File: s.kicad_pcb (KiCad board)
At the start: 2 copper layers, 200 x 77.4 mm, 98 parts, among them J2 UART connector, J4 Conn_01x02_Pin, J5 USB4105-GF-A, SW1 Z, SW10 D, SW11 S, SW12 K, SW13 W, SW14 R, SW15 STAR, SW16 R, SW17 B, SW18 G, SW19 S, SW2 T, SW20 Z, SW21 A, SW22 O, SW23 NUM, SW24 E, SW25 U, SW26 210-4MS, SW27 09.03290.01, SW28 EVP-AA202K, SW3 P, SW4 H, SW5 STAR, SW6 F, SW7 P, SW8 L, SW9 T, U1 ESP32-S3-WROOM-1, U2 MCP1825S, U3 MCP1825S, U4 AP9101CK, U5 MCP73831-2-OT, U6 DMG6968U-7, U7 DMG6968U-7

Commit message: WIP: drafting PCB edges
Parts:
- J2: moved to B.Cu
- moved H4 201.1 mm to (56.6, 131.6)
- moved H3 141.2 mm to (204.7, 131.6)
- moved H1 77.0 mm to (238.9, 63.1)
- moved J2 33.2 mm to (224.4, 95.8)
- moved C4 18.2 mm to (197.4, 117.4)
- moved C2 18.0 mm to (197.4, 115.2)
- moved R3 16.9 mm to (197.4, 119.9)
- moved SW27 16.8 mm to (73.2, 120.7)
- moved J4 15.5 mm to (69.6, 105.6)
- moved J5 10.5 mm to (56.0, 120.3)
- moved C6 8.72 mm to (219.4, 123.8)
- moved U2 8.47 mm to (204.0, 122.2)
- moved C5 8.41 mm to (216.7, 123.8)
- moved R1 8.41 mm to (214.0, 123.8)
- moved C1 8.41 mm to (210.9, 124.8)
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- renumbered H2 to H1, H4 to H2, H5 to H3, H6 to H4
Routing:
- net /battery_mgmt/vbatt_mon: track 193.2 -> 0.00 mm, vias 2 -> 0
- net /VBUS: track 173.1 -> 0.00 mm, vias 2 -> 0
- net Net-(U1-IO16): track 160.7 -> 0.00 mm, vias 2 -> 0
- net /battery_mgmt/3v3_from_batt: track 146.4 -> 0.00 mm, vias 2 -> 0
- net +3.3V: track 129.2 -> 23.1 mm, vias 2 -> 0
- net Net-(U1-IO0): track 72.2 -> 2.68 mm, vias 1 -> 0
- net /sw_2: track 68.7 -> 0.00 mm, vias 1 -> 0
- net /battery_mgmt/HV_CHR: track 68.3 -> 0.00 mm
- net /sw_3: track 66.6 -> 0.00 mm, vias 1 -> 0
- net /sw_4: track 64.1 -> 0.00 mm, vias 1 -> 0
- net /matrix_c5: track 148.2 -> 91.5 mm, vias 1 -> 0
- net /matrix_c4: track 167.1 -> 110.9 mm, vias 1 -> 0
- net /USB_D+: track 183.8 -> 127.7 mm
- net /led_2: track 87.2 -> 31.5 mm, vias 1 -> 0
- net /USB_D-: track 182.6 -> 127.7 mm
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- removed copper zone on B.Cu, net GND
- removed copper zone on F.Cu, net GND
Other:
- board size 200 x 77.4 mm -> 218.3 x 102.6 mm

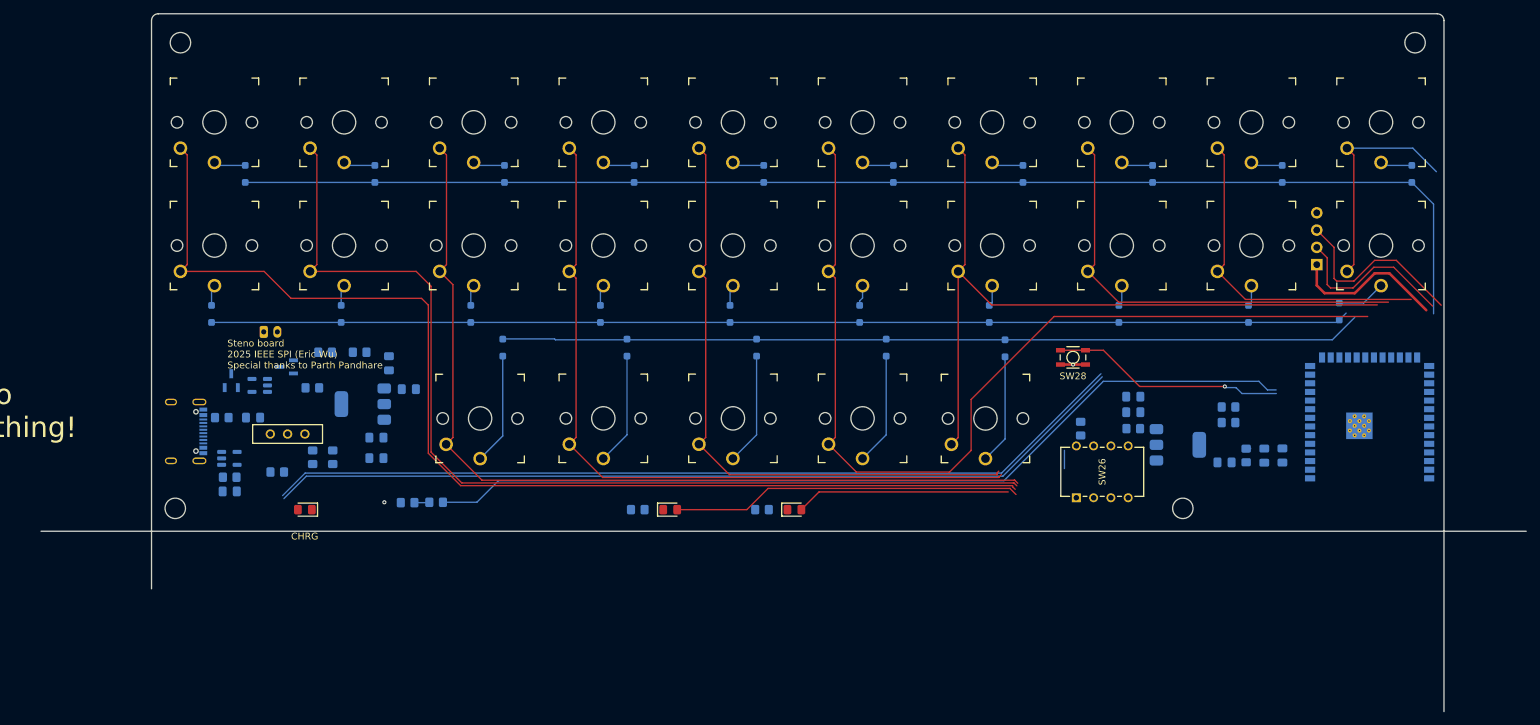
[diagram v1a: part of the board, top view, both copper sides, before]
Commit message: WIP :finalize edge cuts
The new board dimensions are 189.95mm x 76.05mm
with corners of radius 1.00 mm
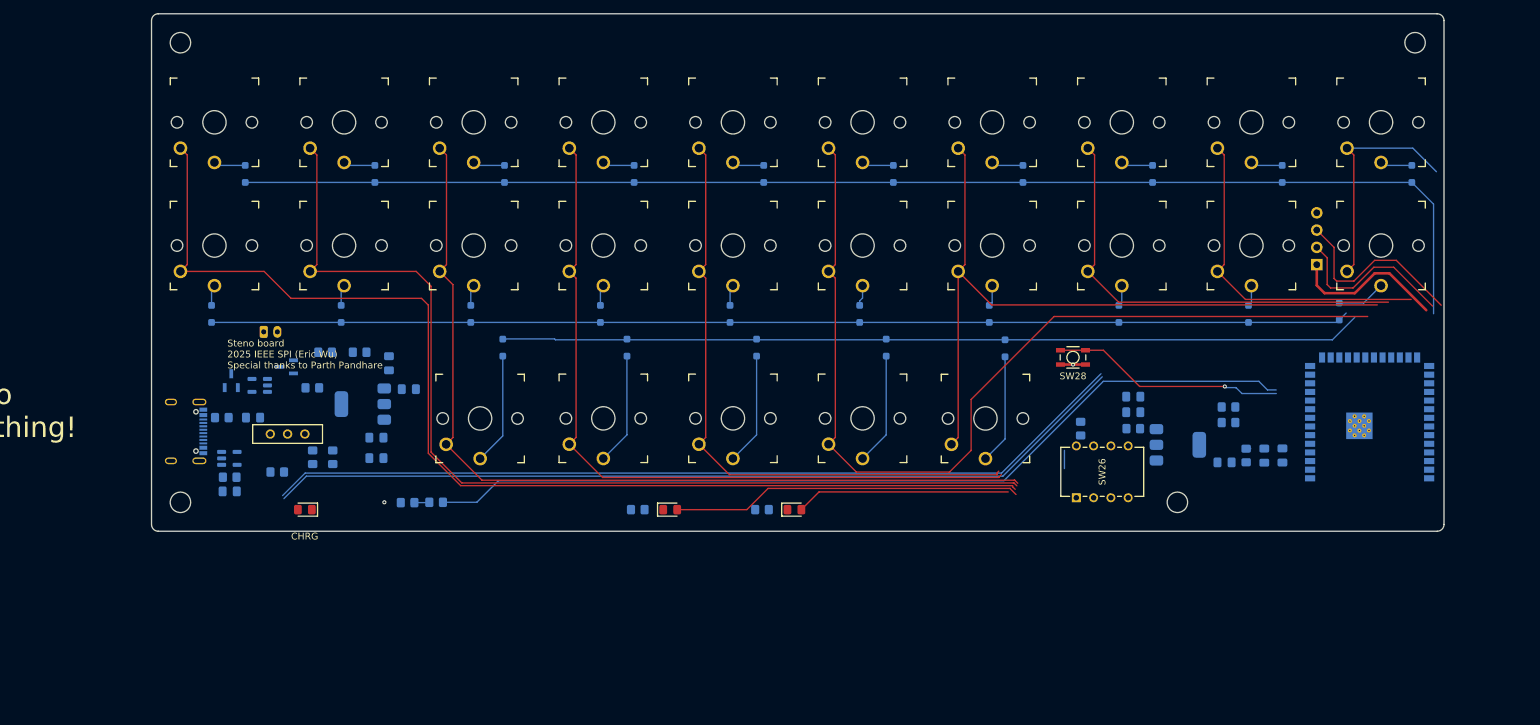
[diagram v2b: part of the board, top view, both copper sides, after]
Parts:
- moved H3 1.19 mm to (203.9, 130.7)
- moved H4 1.17 mm to (57.4, 130.7)
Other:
- board size 218.3 x 102.6 mm -> 190 x 76 mm
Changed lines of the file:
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@@
 	(footprint "MountingHole:MountingHole_3mm"
 		(layer "F.Cu")
-		(at 56.642 131.572)
+		(at 57.404 130.688)
 		(descr "Mounting Hole 3mm, no annular, generated by kicad-footprint-generator mountinghole.py")
 		(tags "mountinghole")
@@
 	(footprint "MountingHole:MountingHole_3mm"
 		(layer "F.Cu")
-		(at 204.724 131.572)
+		(at 203.924 130.688)
 		(descr "Mounting Hole 3mm, no annular, generated by kicad-footprint-generator mountinghole.py")
 		(tags "mountinghole")
@@
 	)
 	(gr_line
-		(start 53.154 143.398875)
+		(start 53.154 133.9375)
 		(end 53.154 59.88775)
 		(stroke
@@
 		(layer "Edge.Cuts")
 	)
+	(gr_arc
+		(start 54.154 134.9375)
+		(mid 53.446893 134.644607)
+		(end 53.154 133.9375)
+		(stroke
+			(width 0.05)
+			(type solid)
+		)
+		(layer "Edge.Cuts")
+	)
 	(gr_line
-		(start 243.104 161.44875)
+		(start 243.104 133.9375)
 		(end 243.104 59.88775)
 		(stroke
@@
 	)
 	(gr_line
-		(start 36.909375 134.9375)
-		(end 255.190625 134.9375)
+		(start 54.154 134.9375)
+		(end 242.104 134.9375)
 		(stroke
 			(width 0.05)
-			(type default)
+			(type solid)
+		)
+		(layer "Edge.Cuts")
+	)
+	(gr_arc
+		(start 243.104 133.9375)
+		(mid 242.811107 134.644607)
+		(end 242.104 134.9375)
+		(stroke
+			(width 0.05)
+			(type solid)
 		)
 		(layer "Edge.Cuts")

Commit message: WIP: routing traces
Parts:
- moved R2 23.6 mm to (212.7, 124.8)
- moved R16 17.4 mm to (96.4, 129.2), turned to 0 degrees
- moved R17 16.2 mm to (92.2, 129.2), turned to 180 degrees
- moved SW27 11.7 mm to (70.7, 109.2)
- moved D25 9.82 mm to (170.8, 114.0)
- moved D20 9.15 mm to (219.5, 98.7)
- moved C1 9.01 mm to (215.3, 117.0), turned to 90 degrees
- moved U7 8.76 mm to (64.6, 113.4), turned to -90 degrees
- moved SW28 8.65 mm to (196.8, 111.9)
- moved D10 7.11 mm to (231.3, 82.4)
- moved D21 6.10 mm to (104.9, 114.0)
- moved D22 6.10 mm to (123.2, 114.0)
- moved D23 6.10 mm to (142.2, 114.0)
- moved D24 6.10 mm to (161.3, 114.0)
- moved R7 5.23 mm to (67.8, 121.2)
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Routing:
- net /battery_mgmt/vbatt_mon: track 0.00 -> 284.5 mm, vias 0 -> 2
- net /VBUS: track 0.00 -> 163.0 mm, vias 0 -> 5
- net Net-(U1-IO16): track 0.00 -> 149.1 mm
- net /battery_mgmt/3v3_from_batt: track 0.00 -> 143.4 mm, vias 0 -> 2
- net GND: track 3.68 -> 140.8 mm, vias 2 -> 5
- net Net-(U1-IO0): track 2.68 -> 72.9 mm, vias 0 -> 2
- net /USB_D+: track 127.7 -> 189.5 mm
- net /USB_D-: track 127.7 -> 188.1 mm, vias 0 -> 2
- net /sw_2: track 0.00 -> 59.6 mm, vias 0 -> 1
- net /sw_3: track 0.00 -> 55.0 mm, vias 0 -> 1
- net /led_2: track 31.5 -> 82.1 mm, vias 0 -> 1
- net /sw_4: track 0.00 -> 50.4 mm, vias 0 -> 1
- net /CC2: track 0.00 -> 50.4 mm
- net /led_1: track 51.5 -> 101.2 mm, vias 0 -> 1
- net /matrix_c4: track 110.9 -> 158.2 mm, vias 0 -> 1
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
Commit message: WIP: more routing done
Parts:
- moved D30 5.62 mm to (71.9, 130.7), turned to 0 degrees
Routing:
- net /matrix_r2: track 161.3 -> 182.0 mm
- net GND: track 140.8 -> 130.2 mm
- net Net-(D30-K): track 11.6 -> 5.34 mm
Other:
- board text added: "Steno board UCLA IEEE SPI (Eric Wu, 2025) Special thanks to Parth Pandhare"
- board text removed: "Steno board 2025 IEEE SPI (Eric Wu) Special thanks to Parth Pandhare"

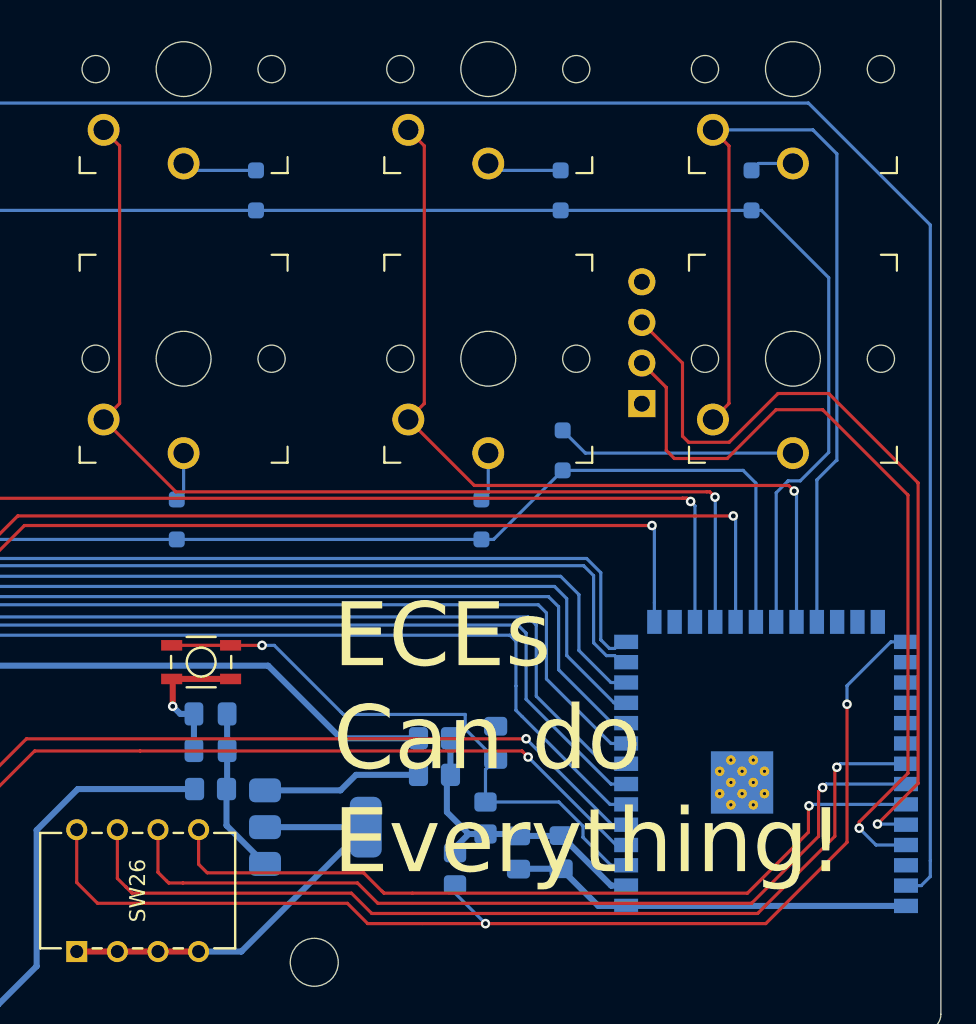
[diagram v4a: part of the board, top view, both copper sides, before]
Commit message: WIP: route everything except ground planes
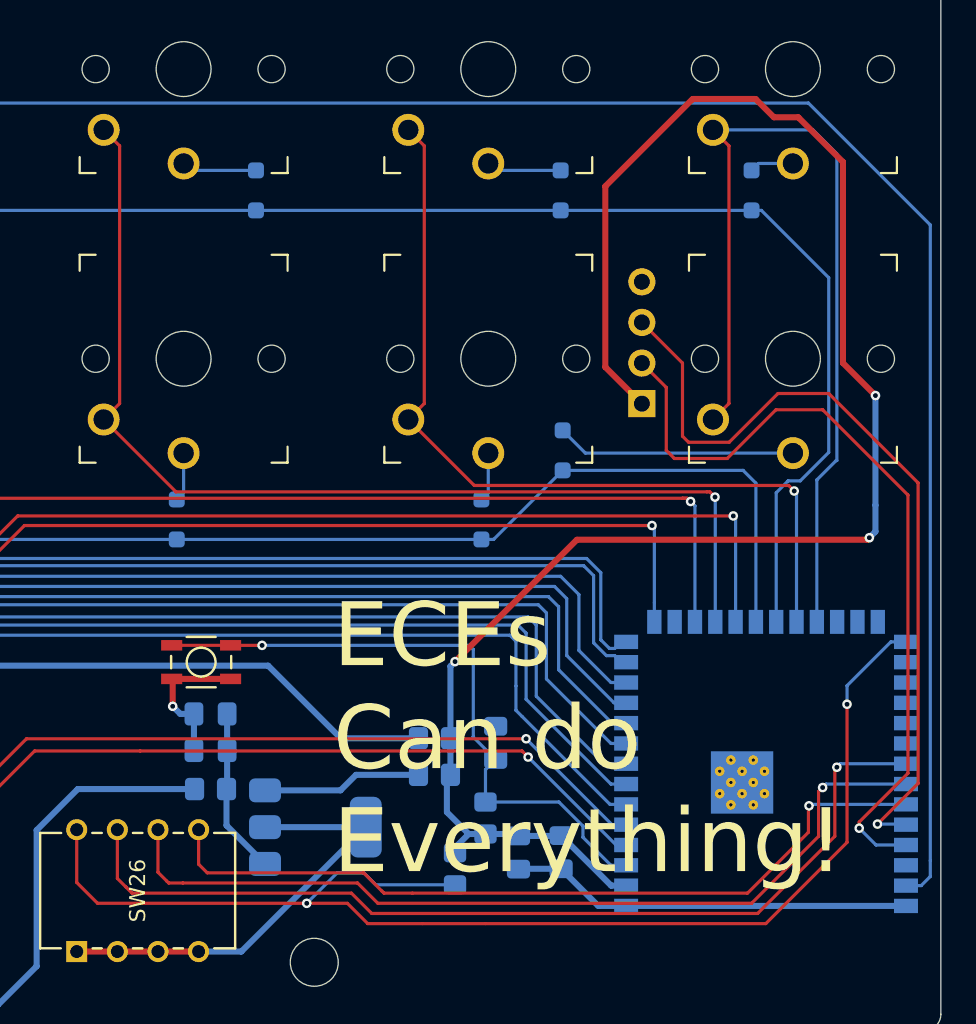
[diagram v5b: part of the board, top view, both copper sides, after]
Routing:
- net +3.3V: track 19.4 -> 111.2 mm, vias 0 -> 3
- net Net-(U1-IO0): track 72.9 -> 80.1 mm
- net Net-(U1-EN): track 37.5 -> 40.2 mm
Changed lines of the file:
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@@
+	)
+	(segment
+		(start 239.014 95.25)
+		(end 236.982 93.218)
+		(width 0.381)
+		(layer "F.Cu")
+		(net 7)
+	)
+	(segment
+		(start 222.123 93.472)
+		(end 224.409 95.758)
+		(width 0.381)
+		(layer "F.Cu")
+		(net 7)
+	)
+	(segment
+		(start 212.725 111.887)
+		(end 218.694 105.918)
+		(width 0.381)
+		(layer "F.Cu")
+		(net 7)
+	)
+	(segment
+		(start 232.664 77.851)
+		(end 231.521 76.708)
+		(width 0.381)
+		(layer "F.Cu")
+		(net 7)
+	)
+	(segment
+		(start 234.188 77.851)
+		(end 232.664 77.851)
+		(width 0.381)
+		(layer "F.Cu")
+		(net 7)
+	)
+	(segment
+		(start 220.345 104.267)
+		(end 232.918 104.267)
+		(width 0.381)
+		(layer "F.Cu")
+		(net 7)
+	)
+	(segment
+		(start 238.506 104.267)
+		(end 238.633 104.14)
+		(width 0.381)
+		(layer "F.Cu")
+		(net 7)
+	)
+	(segment
+		(start 236.982 93.218)
+		(end 236.982 80.645)
+		(width 0.381)
+		(layer "F.Cu")
+		(net 7)
+	)
+	(segment
+		(start 218.694 105.918)
+		(end 220.345 104.267)
+		(width 0.381)
+		(layer "F.Cu")
+		(net 7)
+	)
+	(segment
+		(start 236.982 80.645)
+		(end 234.188 77.851)
+		(width 0.381)
+		(layer "F.Cu")
+		(net 7)
+	)
+	(segment
+		(start 232.918 104.267)
+		(end 238.506 104.267)
+		(width 0.381)
+		(layer "F.Cu")
+		(net 7)
+	)
+	(segment
+		(start 231.521 76.708)
+		(end 227.584 76.708)
+		(width 0.381)
+		(layer "F.Cu")
+		(net 7)
+	)
+	(segment
+		(start 227.584 76.708)
+		(end 222.123 82.169)
+		(width 0.381)
+		(layer "F.Cu")
+		(net 7)
+	)
+	(segment
+		(start 222.123 82.169)
+		(end 222.123 93.472)
+		(width 0.381)
+		(layer "F.Cu")
+		(net 7)
+	)
+	(via
+		(at 238.633 104.14)
+		(size 0.6)
+		(drill 0.3)
+		(layers "F.Cu" "B.Cu")
+		(net 7)
+	)
+	(via
+		(at 239.014 95.25)
+		(size 0.6)
+		(drill 0.3)
+		(layers "F.Cu" "B.Cu")
+		(net 7)
+	)
+	(via
+		(at 212.725 111.887)
+		(size 0.6)
+		(drill 0.3)
+		(layers "F.Cu" "B.Cu")
+		(net 7)
 	)
 	(segment
@@
 	)
 	(segment
+		(start 212.43925 112.17275)
+		(end 212.725 111.887)
+		(width 0.381)
+		(layer "B.Cu")
+		(net 7)
+	)
+	(segment
 		(start 216.67775 122.8035)
 		(end 216.69375 122.7875)
@@
 	)
 	(segment
+		(start 238.633 104.14)
+		(end 239.014 103.759)
+		(width 0.381)
+		(layer "B.Cu")
+		(net 7)
+	)
+	(segment
+		(start 239.014 103.759)
+		(end 239.014 102.108)
+		(width 0.381)
+		(layer "B.Cu")
+		(net 7)
+	)
+	(segment
+		(start 239.014 102.108)
+		(end 239.014 95.25)
+		(width 0.381)
+		(layer "B.Cu")
+		(net 7)
+	)
+	(segment
 		(start 212.217 121.301)
 		(end 212.217 119.1895)
@@
 		(start 216.69375 122.7875)
 		(end 219.33925 122.7875)
+		(width 0.381)
+		(layer "B.Cu")
+		(net 7)
+	)
+	(segment
+		(start 212.43925 116.68125)
+		(end 212.43925 112.17275)
 		(width 0.381)
 		(layer "B.Cu")
@@
 	)
 	(segment
-		(start 205.613 115.062)
-		(end 201.422 110.871)
-		(width 0.2)
-		(layer "B.Cu")
-		(net 8)
-	)
-	(segment
-		(start 201.422 110.871)
-		(end 200.66 110.871)
-		(width 0.2)
-		(layer "B.Cu")
-		(net 8)
-	)
-	(segment
 		(start 220.726 122.876)
 		(end 222.47375 124.62375)
@@
 	)
 	(segment
-		(start 215.265 118.0045)
-		(end 213.36 116.0995)
+		(start 213.868 111.125)
+		(end 213.614 110.871)
 		(width 0.2)
 		(layer "B.Cu")
@@
 	)
 	(segment
-		(start 213.36 116.0995)
-		(end 213.36 115.189)
+		(start 213.868 116.586)
+		(end 213.868 111.125)
 		(width 0.2)
 		(layer "B.Cu")
@@
 	)
 	(segment
-		(start 213.36 115.189)
-		(end 205.74 115.189)
+		(start 213.85725 116.59675)
+		(end 213.868 116.586)
 		(width 0.2)
 		(layer "B.Cu")
@@
 	)
 	(segment
-		(start 205.74 115.189)
-		(end 205.613 115.062)
+		(start 213.614 110.871)
+		(end 200.66 110.871)
+		(width 0.2)
+		(layer "B.Cu")
+		(net 8)
+	)
+	(segment
+		(start 215.265 118.0045)
+		(end 213.85725 116.59675)
 		(width 0.2)
 		(layer "B.Cu")
@@
 	)
 	(segment
-		(start 205.994 127)
+		(start 203.454 127)
 		(end 190.373 127)
 		(width 0.2)
@@
 		(start 207.264 128.27)
 		(end 205.994 127)
+		(width 0.2)
+		(layer "F.Cu")
+		(net 54)
+	)
+	(segment
+		(start 205.994 127)
+		(end 203.454 127)
 		(width 0.2)
 		(layer "F.Cu")
@@
 	)
 	(via
-		(at 214.63 128.27)
+		(at 203.454 127)
 		(size 0.6)
 		(drill 0.3)
@@
 	)
 	(segment
-		(start 212.725 125.841)
-		(end 212.725 126.365)
-		(width 0.2)
-		(layer "B.Cu")
-		(net 54)
-	)
-	(segment
 		(start 239.97375 110.65375)
 		(end 237.236 113.3915)
@@
 	)
 	(segment
+		(start 207.756 125.841)
+		(end 207.01 125.095)
+		(width 0.2)
+		(layer "B.Cu")
+		(net 54)
+	)
+	(segment
 		(start 240.92375 110.65375)
 		(end 240.50125 110.65375)
@@
 	)
 	(segment
-		(start 212.725 126.365)
-		(end 214.63 128.27)
+		(start 205.359 125.095)
+		(end 203.454 127)
+		(width 0.2)
+		(layer "B.Cu")
+		(net 54)
+	)
+	(segment
+		(start 212.725 125.841)
+		(end 207.756 125.841)
 		(width 0.2)
 		(layer "B.Cu")
@@
 		(width 0.2)
 		(layer "B.Cu")
+		(net 54)
+	)
+	(segment
+		(start 207.01 125.095)
+		(end 205.359 125.095)
+		(width 0.2)
+		(layer "B.Cu")
